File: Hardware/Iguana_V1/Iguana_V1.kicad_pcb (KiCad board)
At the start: 2 copper layers, 70 x 75 mm, 113 parts, among them J1 ON OFF, J11 Conn_Coaxial, J12 Conn_Coaxial, J13 HDR-3x1, J14 HDR-3x1, J15 ds18b20, J16 SHT31, J17 HDR-2x1, J18 OLED, J19 NPK/H Sensor, J3 BAT, J4 HDR-2x1, J7 USB_B_Micro, J8 Cap. Moisture Sensor, J9 Conn_01x02, Q1 Q_PMOS_GSD, Q3 Q_Dual_NPN_NPN_BRT_E1B1C2E2B2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, SW1 SW_DIP_x02, SW2 SW_DIP_x02, SW3 SW_DIP_x02, U1 DW01, U10 RV-8803, U11 RFM95W-915S2, U12 MAX3485, U2 TP4056, U3 MT3608, U4 FS8205A, U5 AP2112K-3.3, U6 AP2112K-3.3, U7 AP2112K-3.3, U8 CH340C, U9 ESP32-WROOM-32D

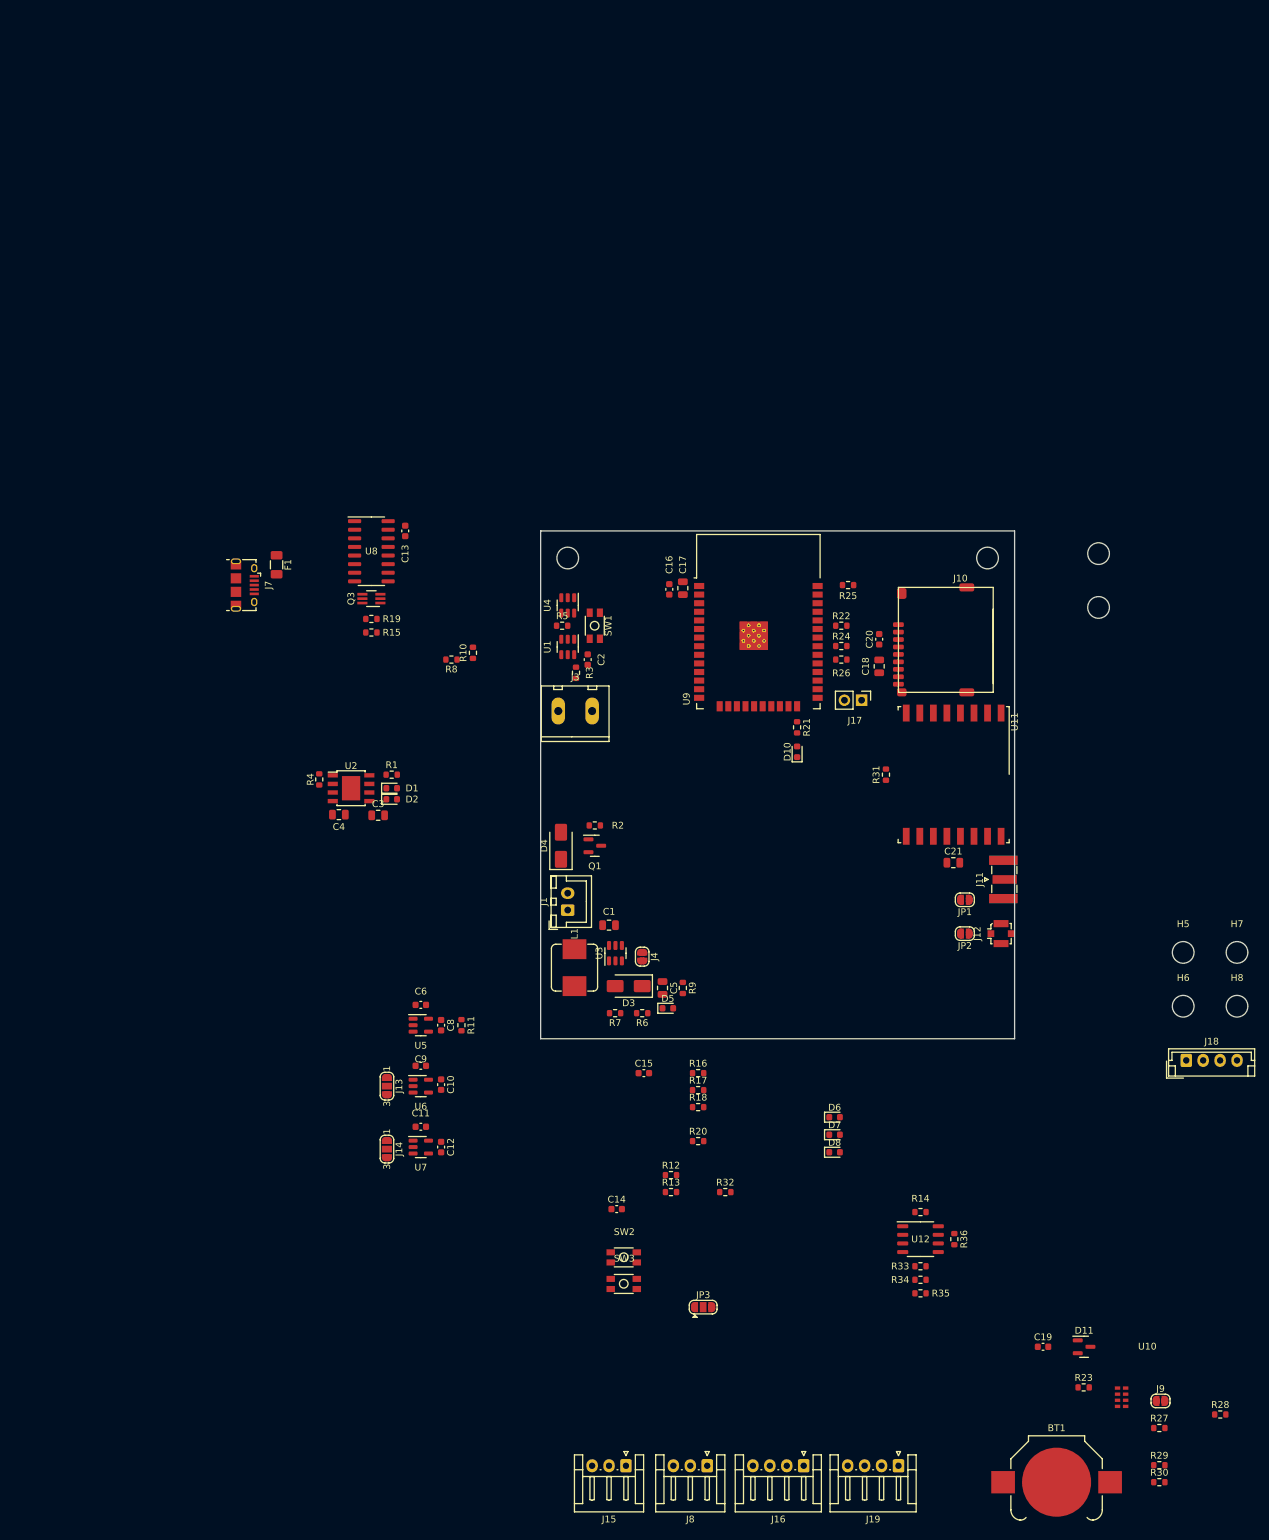
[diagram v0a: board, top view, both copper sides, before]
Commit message: adding relay and working on pcb
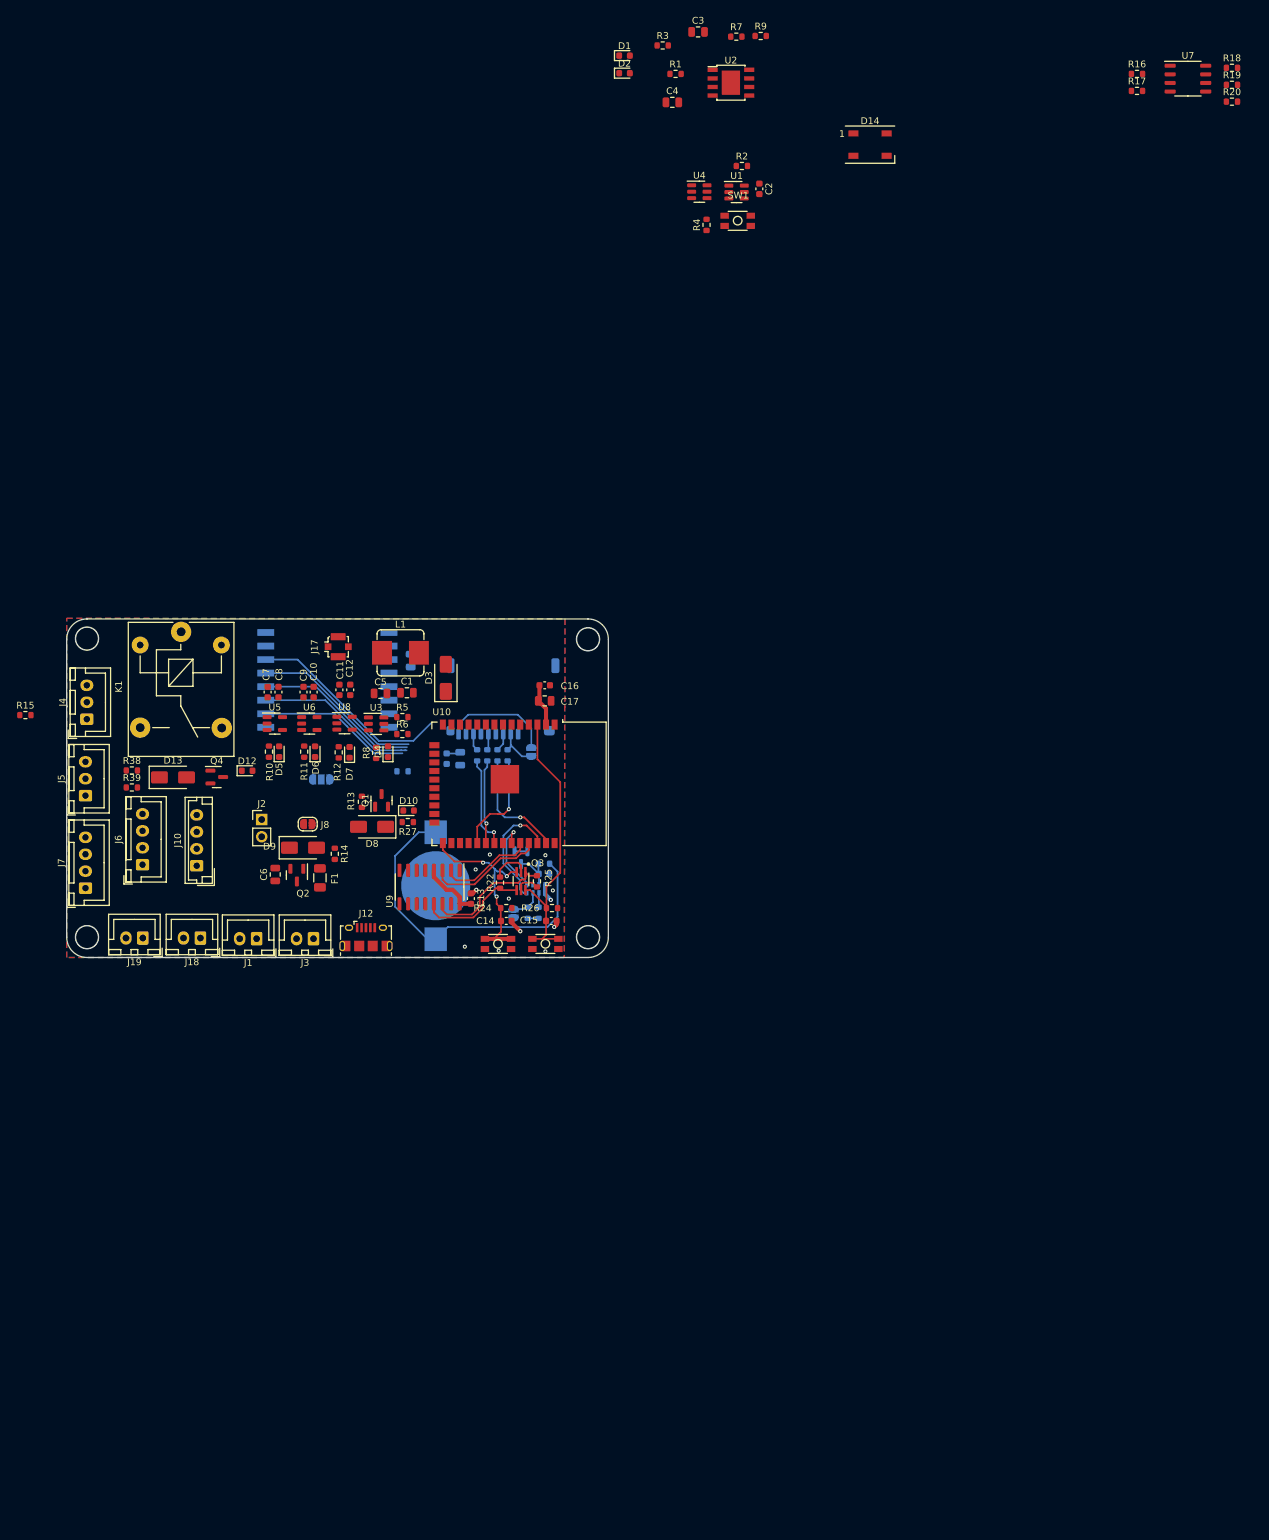
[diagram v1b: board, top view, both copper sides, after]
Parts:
- removed H1, H2, H3, H4, H5, H6, H7, H8: MountingHole, MountingHole:MountingHole_3.2mm_M3
- removed J11: Conn_Coaxial, Connector_Coaxial:SMA_Samtec_SMA-J-P-X-ST-EM1_EdgeMount
- removed J16: SHT31, Connector_JST:JST_EH_S4B-EH_1x04_P2.50mm_Horizontal
- removed JP1, JP2: SolderJumper_2_Open, Jumper:SolderJumper-2_P1.3mm_Open_RoundedPad1.0x1.5mm
- removed JP3: SolderJumper_3_Open, Jumper:SolderJumper-3_P1.3mm_Open_RoundedPad1.0x1.5mm
- removed R21: 330, Resistor_SMD:R_0603_1608Metric
- removed R23: 3.3k, Resistor_SMD:R_0603_1608Metric
- removed R35: 10k, Resistor_SMD:R_0603_1608Metric
- removed R36: 120, Resistor_SMD:R_0603_1608Metric
- added C7: 1u, Capacitor_SMD:C_0603_1608Metric, F.Cu at (109.7, 40.8)
- added D12: LED, LED_SMD:LED_0603_1608Metric, F.Cu at (106.7, 52.4)
- added D13: MRA4007T3G, Diode_SMD:D_SMA, F.Cu at (95.7, 53.4)
- added D14: WS2812B, LED_SMD:LED_WS2812B_PLCC4_5.0x5.0mm_P3.2mm, F.Cu at (198.7, -40.0)
- added D9: D_Schottky, Diode_SMD:D_SMA, F.Cu at (114.9, 63.8)
- added J2: HDR-2x1, Connector_PinHeader_2.54mm:PinHeader_1x02_P2.54mm_Vertical, F.Cu at (108.8, 59.6)
- added J5: ds18b20, Connector_JST:JST_XH_B3B-XH-A_1x03_P2.50mm_Vertical, F.Cu at (82.8, 56.1)
- added J6: SHT31, Connector_JST:JST_XH_B4B-XH-A_1x04_P2.50mm_Vertical, F.Cu at (91.2, 66.3)
- added K1: Relay_SPDT, Relay_THT:Relay_SPDT_SANYOU_SRD_Series_Form_C, F.Cu at (96.9, 31.9)
- added Q2: Q_PMOS_GSD, Package_TO_SOT_SMD:SOT-23, F.Cu at (114.0, 67.8)
- added Q4: MMBT3904, Package_TO_SOT_SMD:SOT-23, F.Cu at (102.2, 53.4)
- added R37: 10k, Resistor_SMD:R_0603_1608Metric, B.Cu at (129.6, 52.5)
- added R38: 330, Resistor_SMD:R_0603_1608Metric, F.Cu at (89.6, 52.4)
- added R39: 10, Resistor_SMD:R_0603_1608Metric, F.Cu at (89.6, 54.9)
- BT1, C18, C19, C20, C21, D11: moved to B.Cu
- C6: value 1u -> 4.7u; footprint Capacitor_SMD:C_0603_1608Metric -> Capacitor_SMD:C_0805_2012Metric
- D4: value D_Schottky -> LED; footprint Diode_SMD:D_SMA -> LED_SMD:LED_0603_1608Metric
- D8: value LED -> D_Schottky; footprint LED_SMD:LED_0603_1608Metric -> Diode_SMD:D_SMA
- J1: value ON OFF -> BAT
- J10: value ~ -> OLED; footprint IoWLabsConnectors:microSD_push_push -> Connector_JST:JST_EH_B4B-EH-A_1x04_P2.50mm_Vertical
- J12: value Conn_Coaxial -> USB_B_Micro; footprint Connector_Coaxial:U.FL_Molex_MCRF_73412-0110_Vertical -> Connector_USB:USB_Micro-B_Amphenol_10118194_Horizontal
- J13: value HDR-3x1 -> HDR-2x1; footprint Jumper:SolderJumper-3_P1.3mm_Open_RoundedPad1.0x1.5mm_NumberLabels -> Jumper:SolderJumper-2_P1.3mm_Open_RoundedPad1.0x1.5mm; moved to B.Cu
- J14: value HDR-3x1 -> Conn_01x02; footprint Jumper:SolderJumper-3_P1.3mm_Open_RoundedPad1.0x1.5mm_NumberLabels -> Jumper:SolderJumper-2_P1.3mm_Open_RoundedPad1.0x1.5mm; moved to B.Cu
- J15: value ds18b20 -> ~; footprint Connector_JST:JST_EH_S3B-EH_1x03_P2.50mm_Horizontal -> IoWLabsConnectors:microSD_push_push; moved to B.Cu
- J17: value HDR-2x1 -> Conn_Coaxial; footprint Connector_PinHeader_2.54mm:PinHeader_1x02_P2.54mm_Vertical -> Connector_Coaxial:U.FL_Molex_MCRF_73412-0110_Vertical
- J18: value OLED -> IN; footprint Connector_JST:JST_EH_B4B-EH-A_1x04_P2.50mm_Vertical -> Connector_JST:JST_XH_B2B-XH-A_1x02_P2.50mm_Vertical
- J19: value NPK/H Sensor -> IN; footprint Connector_JST:JST_EH_S4B-EH_1x04_P2.50mm_Horizontal -> Connector_JST:JST_XH_B2B-XH-A_1x02_P2.50mm_Vertical
- J3: value BAT -> IN; footprint IoWLabsConnectors:Tb-2x1-5p-TH-V -> Connector_JST:JST_XH_B2B-XH-A_1x02_P2.50mm_Vertical
- J4: value HDR-2x1 -> Cap. Moisture Sensor; footprint Jumper:SolderJumper-2_P1.3mm_Open_RoundedPad1.0x1.5mm -> Connector_JST:JST_XH_B3B-XH-A_1x03_P2.50mm_Vertical
- J7: value USB_B_Micro -> NPK/H Sensor; footprint Connector_USB:USB_Micro-B_Amphenol_10118194_Horizontal -> Connector_JST:JST_XH_B4B-XH-A_1x04_P2.50mm_Vertical
- J8: value Cap. Moisture Sensor -> ON OFF; footprint Connector_JST:JST_EH_S3B-EH_1x03_P2.50mm_Horizontal -> Jumper:SolderJumper-2_P1.3mm_Open_RoundedPad1.0x1.5mm
- J9: value Conn_01x02 -> HDR-3x1; footprint Jumper:SolderJumper-2_P1.3mm_Open_RoundedPad1.0x1.5mm -> Jumper:SolderJumper-3_P1.3mm_Open_RoundedPad1.0x1.5mm_NumberLabels; moved to B.Cu
- R10: value 30K -> 1k
- R13: value 1k -> 10K
- R14: value 10k -> 10K
- R15: value 10K -> 4.7K
- R16: value 200 -> 120
- R17: value 200 -> 10k
- R18, R19, R20: value 10K -> 10k
- R2: value 10K -> 100
- R22, R24, R25, R26: value 3.3k -> 10K
- R27: value 100k -> 330
- R28: value 100k -> 3.3k; moved to B.Cu
- R29, R30: value 2.2k -> 3.3k; moved to B.Cu
- R3: value 100 -> 1K2
- R31: value 10k -> 3.3k; moved to B.Cu
- R32: value 4.7K -> 3.3k; moved to B.Cu
- R33, R34: value 10k -> 100k; moved to B.Cu
- R4: value 1K2 -> 1K
- R5: value 1K -> 7K5
- R6: value 7K5 -> 1K
- R7: value 1K -> 12K
- R8: value 12K -> 470
- R9: value 470 -> 30K
- U10: value RV-8803 -> ESP32-WROOM-32D; footprint IoWLabs:SON-8 -> RF_Module:ESP32-WROOM-32
- U11: value RFM95W-915S2 -> RV-8803; footprint RF_Module:HOPERF_RFM69HW -> IoWLabs:SON-8; moved to B.Cu
- U12: value MAX3485 -> RFM95W-915S2; footprint Package_SO:SOP-8_3.9x4.9mm_P1.27mm -> RF_Module:HOPERF_RFM69HW; moved to B.Cu
- U7: value AP2112K-3.3 -> MAX3485; footprint Package_TO_SOT_SMD:SOT-23-5 -> Package_SO:SOP-8_3.9x4.9mm_P1.27mm
- U8: value CH340C -> AP2112K-3.3; footprint Package_SO:SOIC-16_3.9x9.9mm_P1.27mm -> Package_TO_SOT_SMD:SOT-23-5
- U9: value ESP32-WROOM-32D -> CH340C; footprint RF_Module:ESP32-WROOM-32 -> Package_SO:SOIC-16_3.9x9.9mm_P1.27mm
- moved U7 194.3 mm to (245.6, -49.8)
- moved R20 172.6 mm to (252.1, -46.4)
- moved R18 172.6 mm to (252.1, -51.4)
- moved R17 161.2 mm to (238.1, -48.0)
- moved R16 161.2 mm to (238.1, -50.5)
- moved J9 154.2 mm to (117.6, 53.7), turned to 180 degrees
- moved R19 149.6 mm to (252.1, -48.9)
- moved J18 146.7 mm to (99.8, 77.1), turned to 180 degrees
- moved R28 146.7 mm to (140.6, 50.1), turned to 90 degrees
- moved R30 146.2 mm to (142.1, 50.1), turned to 90 degrees
- moved R7 145.3 mm to (178.9, -56.0), turned to 0 degrees
- moved R27 142.6 mm to (130.4, 60.0), turned to 180 degrees
- moved R9 141.1 mm to (182.5, -56.1), turned to 0 degrees
- moved J19 136.1 mm to (91.2, 77.1)
- moved U10 129.1 mm to (143.8, 54.4), turned to -90 degrees
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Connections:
- C4 pad 1: /V_USB -> /Vin_main
- C6 pad 1: +5V -> /VIN_5V
- D4 pad 1: Net-(D4-K) -> GND
- D4 pad 2: /V_USB -> Net-(D4-A)
- D8 pad 1: GND -> /V1
- D8 pad 2: Net-(D8-A) -> /Vin_main
- J1 pad 1: /V1 -> /BAT+
- J1 pad 2: Net-(D4-K) -> /BAT-
- J10 pad 1: unconnected-(J10-Dat2-Pad1) -> GND
- J10 pad 2: /Dat3 -> /VS_3V3
- J10 pad 3: Net-(J10-CMD) -> /SCL
- J10 pad 4: /VDL_3V3 -> /SDA
- J12 pad 1: Net-(J12-In) -> /V_in
- J12 pad 2: GND -> Net-(J12-D-)
- J13 pad 1: +5V -> /C/D
- J13 pad 2: /EN_VDL_S -> /Dat3
- J14 pad 1: +5V -> /EVI
- J14 pad 2: /EN_VS_S -> GND
- J15 pad 1: GND -> unconnected-(J15-Dat2-Pad1)
- J15 pad 2: /VS_3V3 -> /Dat3
- J15 pad 3: /temp -> Net-(J15-CMD)
- J17 pad 1: /C/D -> Net-(J17-In)
- J17 pad 2: /Dat3 -> GND
- J18 pad 1: GND -> /PUMP_IN-
- J18 pad 2: /VS_3V3 -> /PUMP_IN+
- J19 pad 1: +5V -> /PUMP_IN-
- J19 pad 2: /Data_A -> /PUMP_OUT+
- J3 pad 1: /BAT+ -> GND
- J3 pad 2: /BAT- -> /VIN_5V
- J4 pad 1: +5V -> GND
- J4 pad 2: /Vo_DCDC -> /VS_3V3
- J7 pad 1: /V_in -> +5V
- J7 pad 2: Net-(J7-D-) -> /Data_A
- J7 pad 3: Net-(J7-D+) -> /Data_B
- J7 pad 4: unconnected-(J7-ID-Pad4) -> GND
- J8 pad 1: GND -> /V_USB
- J8 pad 2: /VS_3V3 -> /Vin_main
- J9 pad 1: /EVI -> +5V
- J9 pad 2: GND -> /V_EN
- Q1 pad 1: /V_USB -> /Vin_main
- Q1 pad 2: Net-(D4-K) -> /V1
- R1 pad 1: /V_USB -> /Vin_main
- R10 pad 1: /BAT_LVL -> +3V3
- R10 pad 2: GND -> Net-(D5-A)
- R11 pad 1: +3V3 -> /VDL_3V3
- R12 pad 1: /VDL_3V3 -> /VS_3V3
- R13 pad 1: /VS_3V3 -> /Vin_main
- R13 pad 2: Net-(D8-A) -> GND
- R14 pad 1: /VS_3V3 -> /V_USB
- R14 pad 2: /tx_aux -> GND
- R15 pad 1: /DTR# -> /SENS_TEMP
- R15 pad 2: Net-(Q3B-B1) -> /VS_3V3
- R16 pad 1: /IO0 -> /Data_B
- R16 pad 2: Net-(R16-Pad2) -> /Data_A
- R17 pad 1: /RESET -> /VS_3V3
- R17 pad 2: Net-(R17-Pad2) -> /RS485_TX
- R18 pad 1: +3V3 -> /VS_3V3
- R18 pad 2: /IO0 -> /RS485_EN
- R19 pad 1: Net-(Q3A-B1) -> /VS_3V3
- R19 pad 2: /RST# -> /RS485_EN
- R2 pad 1: /V_USB -> /BAT+
- R2 pad 2: GND -> Net-(U1-VCC)
- R20 pad 1: +3V3 -> /VS_3V3
- R20 pad 2: /RESET -> /RS485_RX
- R22 pad 1: /spi_miso -> /DTR#
- R22 pad 2: Net-(J10-Dat0) -> Net-(Q3B-B1)
- R24 pad 1: /spi_clk -> +3V3
- R24 pad 2: Net-(J10-CLK) -> /IO0
- R25 pad 1: /spi_mosi -> Net-(Q3A-B1)
- R25 pad 2: Net-(J10-CMD) -> /RST#
- R26 pad 1: /SD_cs -> +3V3
- R26 pad 2: /Dat3 -> /RESET
- R27 pad 1: /VDL_3V3 -> /IO2
- R27 pad 2: /INT -> Net-(D10-A)
- R28 pad 1: /VDL_3V3 -> /SPI1_MISO
- R28 pad 2: /EVI -> Net-(J15-Dat0)
- R29 pad 1: /VDL_3V3 -> Net-(D11-K)
- R29 pad 2: /SCL -> Net-(BT1-+)
- R3 pad 1: /BAT+ -> GND
- R3 pad 2: Net-(U1-VCC) -> Net-(U2-PROG)
- R30 pad 1: /VDL_3V3 -> /SPI1_CLK
- R30 pad 2: /SDA -> Net-(J15-CLK)
- R31 pad 1: +3V3 -> /SPI1_MOSI
- R31 pad 2: /rfm_rst -> Net-(J15-CMD)
- R32 pad 1: /temp -> /SD_CS
- R32 pad 2: /VS_3V3 -> /Dat3
- R33 pad 1: /VS_3V3 -> /VDL_3V3
- R33 pad 2: /RS_EN_CH1 -> /INT
- R34 pad 1: /VS_3V3 -> /VDL_3V3
- R34 pad 2: /RS_EN_CH1 -> /EVI
- R4 pad 2: Net-(U2-PROG) -> /CS
- R5 pad 1: GND -> /Vo_DCDC
- R5 pad 2: /CS -> /FB_5V
- R6 pad 1: /Vo_DCDC -> /FB_5V
- R6 pad 2: /FB_5V -> GND
- R7 pad 1: /FB_5V -> /BAT_LVL
- R7 pad 2: GND -> /BAT+
- R8 pad 1: /BAT_LVL -> /Vo_DCDC
- R8 pad 2: /BAT+ -> Net-(D4-A)
- R9 pad 1: /Vo_DCDC -> /BAT_LVL
- R9 pad 2: Net-(D5-A) -> GND
- SW2 pad 3: Net-(R16-Pad2) -> /IO0
- SW2 pad 4: Net-(R16-Pad2) -> /IO0
- SW3 pad 3: Net-(R17-Pad2) -> /RESET
- SW3 pad 4: Net-(R17-Pad2) -> /RESET
- U10 pad 1: /SDA -> GND
- U10 pad 2: unconnected-(U10-CLKOUT-Pad2) -> +3V3
- U10 pad 3: Net-(D11-K) -> /RESET
- U10 pad 4: GND -> unconnected-(U10-SENSOR_VP-Pad4)
- U10 pad 5: GND -> unconnected-(U10-SENSOR_VN-Pad5)
- U10 pad 6: /INT -> /SENS_M
- U10 pad 7: /EVI -> /BAT_LVL
- U10 pad 8: /SCL -> /SENS_TEMP
- U11 pad 1: GND -> /SDA
- U11 pad 2: /spi_miso -> unconnected-(U11-CLKOUT-Pad2)
- U11 pad 3: /spi_mosi -> Net-(D11-K)
- U11 pad 4: /spi_clk -> GND
- U11 pad 5: /rfm_cs -> GND
- U11 pad 6: /rfm_rst -> /INT
- U11 pad 7: unconnected-(U11-DIO5-Pad7) -> /EVI
- U11 pad 8: GND -> /SCL
- U12 pad 1: /tx_aux -> GND
- U12 pad 2: /RS_EN_CH1 -> /SPI1_MISO
- U12 pad 3: /RS_EN_CH1 -> /SPI1_MOSI
- U12 pad 4: /rx_aux -> /SPI1_CLK
- U12 pad 5: GND -> /LORA_CS
- U12 pad 6: /Data_A -> /LORA_RST
- U12 pad 7: /Data_B -> unconnected-(U12-DIO5-Pad7)
- U12 pad 8: /VS_3V3 -> GND
- U2 pad 4: /V_USB -> /Vin_main
- U2 pad 8: /V_USB -> /Vin_main
- U6 pad 3: /EN_VDL_S -> /EN_VDS/S
- U7 pad 1: +5V -> /RS485_TX
- U7 pad 2: GND -> /RS485_EN
- U7 pad 3: /EN_VS_S -> /RS485_EN
- U7 pad 4: unconnected-(U7-NC-Pad4) -> /RS485_RX
- U7 pad 5: /VS_3V3 -> GND
- U8 pad 1: GND -> +5V
- U8 pad 2: /RX -> GND
- U8 pad 3: /TX -> /EN_VDS/S
- U8 pad 4: +3V3 -> unconnected-(U8-NC-Pad4)
- U8 pad 5: Net-(J7-D+) -> /VS_3V3
- U9 pad 10: /rx_aux -> unconnected-(U9-~{DSR}-Pad10)
- U9 pad 11: /tx_aux -> unconnected-(U9-~{RI}-Pad11)
- U9 pad 13: /rfm_dio1 -> /DTR#
- U9 pad 14: unconnected-(U9-IO12-Pad14) -> /RST#
- U9 pad 15: GND -> unconnected-(U9-R232-Pad15)
- U9 pad 16: /rfm_dio0 -> +3V3
- U9 pad 2: +3V3 -> /RX
- U9 pad 3: /RESET -> /TX
- U9 pad 4: unconnected-(U9-SENSOR_VP-Pad4) -> +3V3
- U9 pad 5: unconnected-(U9-SENSOR_VN-Pad5) -> Net-(J12-D+)
- U9 pad 6: unconnected-(U9-IO34-Pad6) -> Net-(J12-D-)
- U9 pad 7: /BAT_LVL -> unconnected-(U9-NC-Pad7)
- U9 pad 8: /RS_EN_CH1 -> unconnected-(U9-NC-Pad8)
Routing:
- net Net-(BT1-+): track 0.00 -> 50.6 mm
- net /RESET: track 0.00 -> 42.4 mm
- net /SPI1_MOSI: track 0.00 -> 40.7 mm, vias 0 -> 1
- net /SPI1_CLK: track 0.00 -> 37.0 mm, vias 0 -> 1
- net /SPI1_MISO: track 0.00 -> 36.3 mm, vias 0 -> 1
- net /LORA_RST: track 0.00 -> 30.4 mm
- net /IO0: track 0.00 -> 28.8 mm, vias 0 -> 3
- net /LORA_CS: track 0.00 -> 25.4 mm
- net /RST#: track 0.00 -> 19.8 mm
- net /TX: track 0.00 -> 17.5 mm
- net /SCL: track 0.00 -> 17.5 mm, vias 0 -> 1
- net /DTR#: track 0.00 -> 16.7 mm
- net /C/D: track 0.00 -> 16.4 mm
- net /SD_CS: track 0.00 -> 16.0 mm, vias 0 -> 1
- net +3V3: track 0.00 -> 15.1 mm
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- added copper zone on B.Cu, net GND
- added copper zone on F.Cu, net GND
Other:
- board size 70 x 75 mm -> 80 x 50 mm

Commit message: replace relay. working on pcb
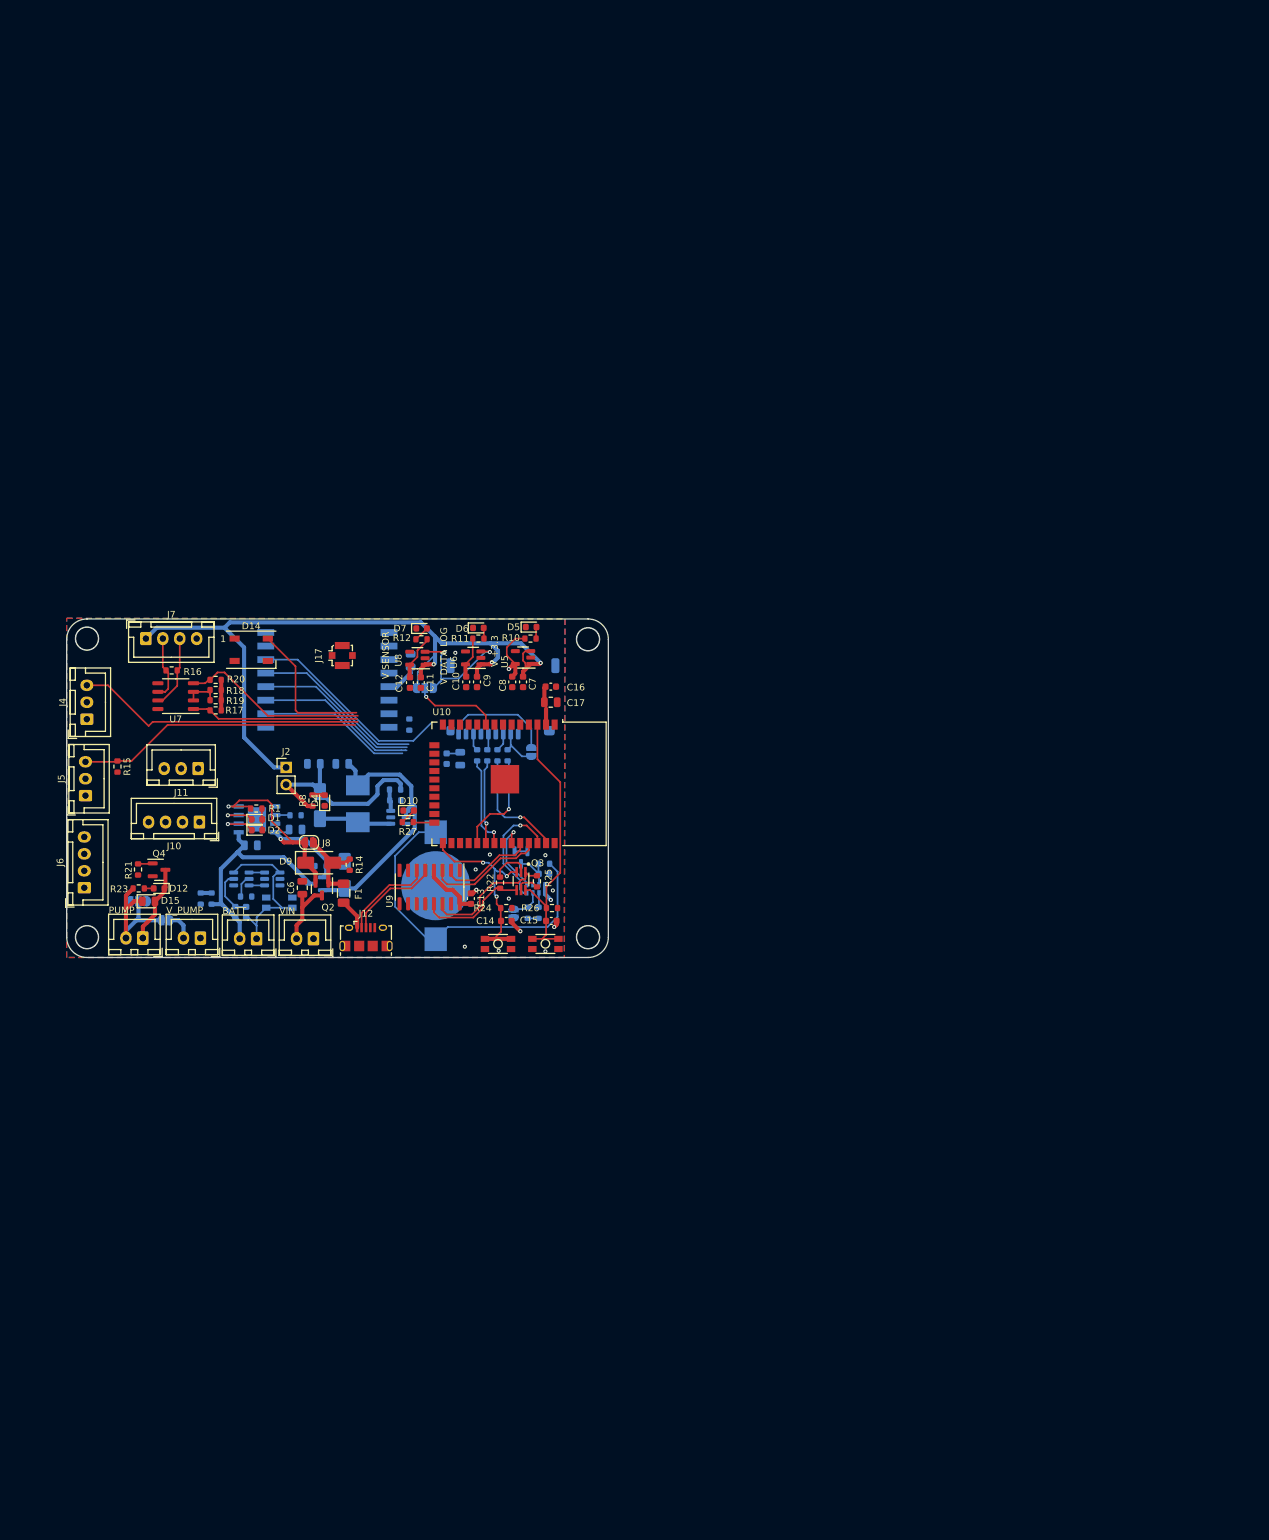
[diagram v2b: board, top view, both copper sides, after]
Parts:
- removed D13: MRA4007T3G, Diode_SMD:D_SMA
- removed K1: Relay_SPDT, Relay_THT:Relay_SPDT_SANYOU_SRD_Series_Form_C
- removed R38: 330, Resistor_SMD:R_0603_1608Metric
- removed R39: 10, Resistor_SMD:R_0603_1608Metric
- added D15: CD4148W, Diode_SMD:D_0805_2012Metric, F.Cu at (92.1, 71.7)
- added J11: rgb led, Connector_JST:JST_XH_B3B-XH-A_1x03_P2.50mm_Vertical, F.Cu at (99.4, 52.1)
- added JP1: SolderJumper_3_Open, Jumper:SolderJumper-3_P1.3mm_Open_RoundedPad1.0x1.5mm, B.Cu at (90.6, 71.7)
- added JP2: SolderJumper_2_Open, Jumper:SolderJumper-2_P1.3mm_Open_RoundedPad1.0x1.5mm, B.Cu at (94.6, 74.5)
- added R21: 10k, Resistor_SMD:R_0603_1608Metric, F.Cu at (90.5, 67.0)
- added R23: 1k, Resistor_SMD:R_0603_1608Metric, F.Cu at (90.6, 69.8)
- C1, C2, C3, C4, C5, D3, D8, L1, Q1, R13, R2, R3, R4, R5, R6, R7, R9, SW1, U1, U2, U3, U4: moved to B.Cu
- J10: footprint Connector_JST:JST_EH_B4B-EH-A_1x04_P2.50mm_Vertical -> Connector_JST:JST_XH_B4B-XH-A_1x04_P2.50mm_Vertical
- Q4: value MMBT3904 -> BSS138
- moved R18 176.0 mm to (102.0, 40.5), turned to 180 degrees
- moved R19 175.5 mm to (102.0, 42.0), turned to 180 degrees
- moved U7 175.1 mm to (96.1, 41.4), turned to 180 degrees
- moved R20 172.7 mm to (102.0, 39.0), turned to 180 degrees
- moved R16 167.6 mm to (95.5, 37.6), turned to 180 degrees
- moved R17 164.0 mm to (102.0, 43.5), turned to 180 degrees
- moved R9 151.9 mm to (99.8, 71.3), turned to -90 degrees
- moved R7 149.0 mm to (101.4, 71.3), turned to -90 degrees
- moved C3 137.1 mm to (107.2, 63.4)
- moved R2 133.2 mm to (104.9, 73.3), turned to 90 degrees
- moved C2 131.0 mm to (106.5, 73.3)
- moved U2 129.4 mm to (108.1, 59.6), turned to 180 degrees
- moved R3 126.0 mm to (113.8, 59.0), turned to 180 degrees
- moved D1 125.2 mm to (108.1, 59.6)
- moved U1 125.1 mm to (105.8, 68.4), turned to 180 degrees
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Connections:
- D12 pad 1: Net-(D12-K) -> /PUMP_OUT-
- D12 pad 2: /VS_3V3 -> Net-(D12-A)
- J1 pad 1: /BAT+ -> /BAT-
- J1 pad 2: /BAT- -> /BAT+
- J18 pad 1: /PUMP_IN- -> GND
- J19 pad 1: /PUMP_IN- -> /PUMP_OUT-
- Q4 pad 1: unconnected-(Q4-B-Pad1) -> /PUMP
- Q4 pad 3: Net-(D13-A) -> /PUMP_OUT-
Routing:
- net +5V: track 0.00 -> 116.1 mm, vias 0 -> 3
- net /Vin_main: track 0.00 -> 45.6 mm, vias 0 -> 2
- net /SENS_M: track 0.00 -> 42.8 mm
- net /SENS_TEMP: track 0.00 -> 42.1 mm
- net /V1: track 0.00 -> 39.2 mm
- net /BAT+: track 0.00 -> 32.9 mm
- net /Vo_DCDC: track 0.00 -> 30.7 mm
- net /RS485_RX: track 0.00 -> 27.4 mm
- net /BAT-: track 0.00 -> 25.6 mm
- net /RS485_TX: track 0.00 -> 24.7 mm
- net /RGB: track 0.00 -> 21.4 mm
- net /PUMP_OUT+: track 0.00 -> 20.6 mm
- net /EN_VDS/S: track 0.00 -> 19.5 mm, vias 0 -> 2
- net Net-(J12-D+): track 0.00 -> 13.9 mm
- net Net-(J12-D-): track 0.00 -> 13.7 mm
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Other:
- board text added: "BATT"
- board text added: "PUMP"
- board text added: "V +3.3"
- board text added: "V DATA LOG"
- board text added: "V SENSOR"
- board text added: "VIN"
- board text added: "V_PUMP"

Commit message: pcb almost ready
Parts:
- moved J4 11.4 mm to (82.6, 56.1)
- moved J5 11.4 mm to (82.7, 44.8)
- moved R15 10.1 mm to (87.3, 41.7)
- moved J17 1.28 mm to (120.2, 34.2), turned to 90 degrees
- moved U10 0.37 mm to (144.2, 54.2)
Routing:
- net +3V3: track 27.9 -> 173.9 mm, vias 1 -> 8
- net /VS_3V3: track 11.2 -> 112.3 mm, vias 0 -> 2
- net /SCL: track 17.5 -> 98.3 mm
- net /SDA: track 11.2 -> 90.8 mm
- net /VDL_3V3: track 11.7 -> 90.1 mm, vias 0 -> 4
- net /PUMP: track 2.19 -> 60.7 mm
- net /RS485_EN: track 5.32 -> 59.8 mm, vias 0 -> 2
- net /SENS_TEMP: track 42.1 -> 68.0 mm
- net /RS485_RX: track 27.4 -> 53.0 mm, vias 0 -> 2
- net /RS485_TX: track 24.7 -> 49.7 mm, vias 0 -> 2
- net /SENS_M: track 42.8 -> 66.4 mm
- net /LORA_D0: track 0.00 -> 19.8 mm, vias 0 -> 1
- net /LORA_D1: track 0.00 -> 18.3 mm, vias 0 -> 1
- net /RBG: track 0.00 -> 14.9 mm
- net GND: track 6.73 -> 15.8 mm, vias 13 -> 27
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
